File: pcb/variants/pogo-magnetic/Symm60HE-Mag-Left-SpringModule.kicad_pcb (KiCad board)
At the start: 2 copper layers, 32 x 18 mm, 2 parts

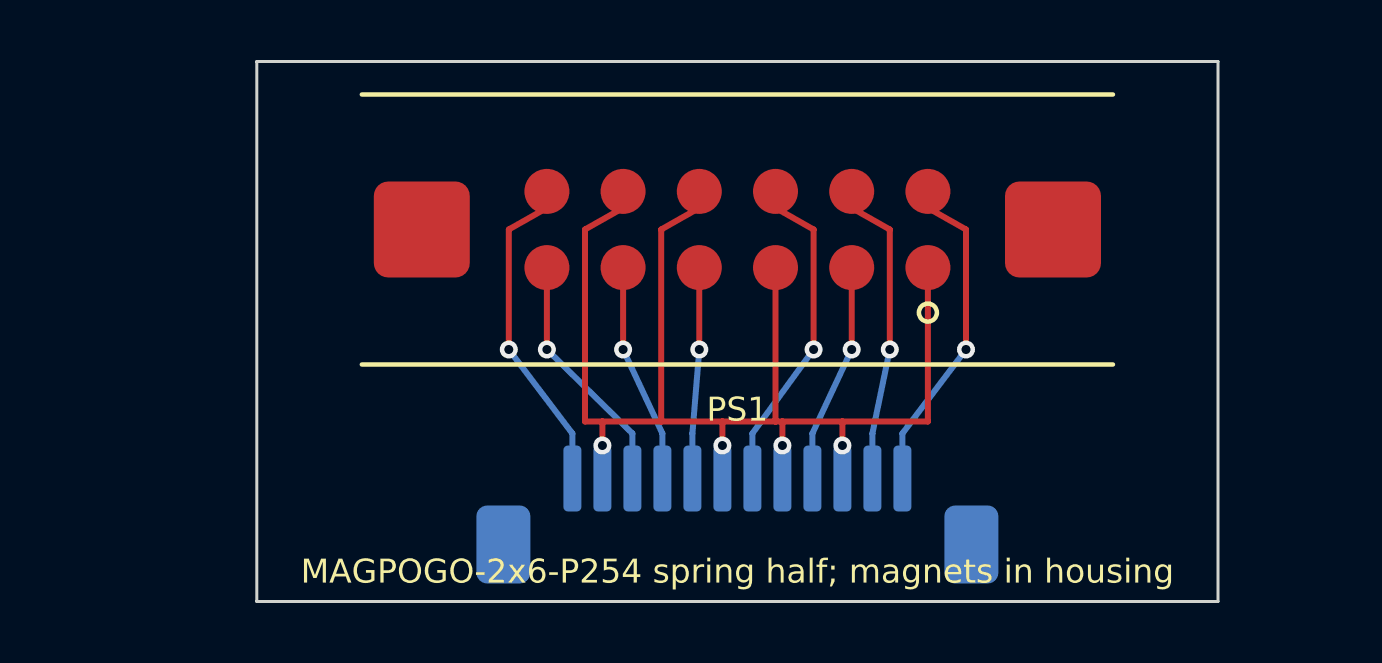
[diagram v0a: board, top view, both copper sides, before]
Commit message: Rebuild the magnetic variant around SUNMON 903-00081
Replaces the invented MAGPOGO-2x6-P254 interface drawing with a real part:
SUNMON 903-00081 / 904-00080 (MC142-09R), nine contacts in two staggered rows
on 1.50 mm pitch with 1.25 mm between rows, 1.20 mm contacts, 0.50 mm DIP
tails, and N52 magnets internal to the housing keyed N to S. Every footprint
dimension is read off the two published drawings.

Nine contacts is the link's functional minimum -- four ADC channels, three mux
selects, +3V3A and one ground -- so the twelve-way interface's four separate
grounds collapse to one and the module ties the controller ZIF's four ground
pads to that single contact.

The stagger is the hard part and it is the part's, not this attempt's:
diagonal neighbours are 1.458 mm apart with 1.25 mm pads, so nothing routes
between the contacts and every run leaves the array at its perimeter. The row
facing the ZIF drops straight to B.Cu; the other takes F.Cu over the top, down
the module side and back in above the ZIF.

Routing is not finished: 6 and 4 clearance flags on the modules, 11 on each
half. Recorded in the README along with why. Footprints, land pattern, pinout
and module outline are settled; the fanout is not.

Modules are 26 x 16 mm. docs/img/42 redraws them and docs/img/43 adds the
target breakout on the Hall PCBs.

Co-Authored-By: Claude Opus 5 <noreply@anthropic.com>
Claude-Session: https://claude.ai/code/session_01CRkZ4zVz5Mq7Fa3C5HAmii
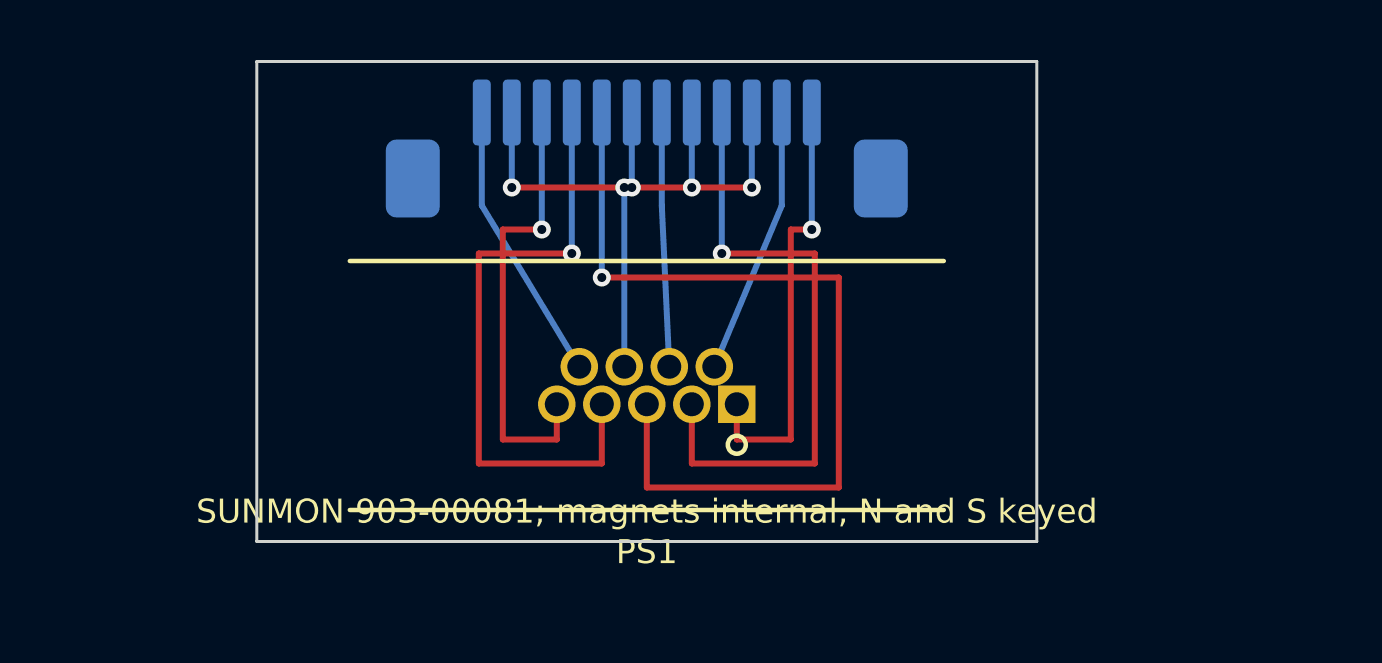
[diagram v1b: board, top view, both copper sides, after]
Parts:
- PS1: value MAGPOGO-2x6-P254-S -> 903-00081; footprint MagPogo_2x6_P254_Spring -> MagPogo_9_MC142_Spring
- moved JF1 12.6 mm to (13.0, 2.80)
- moved PS1 6.01 mm to (13.0, 10.8)
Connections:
- PS1 pad 1: GND -> ADC_L4
- PS1 pad 3: GND -> MUX_A2
- PS1 pad 4: MUX_A2 -> MUX_A1
- PS1 pad 5: MUX_A1 -> MUX_A0
- PS1 pad 6: MUX_A0 -> ADC_L3
- PS1 pad 7: ADC_L4 -> ADC_L1
- PS1 pad 8: ADC_L3 -> GND
- PS1 pad 9: ADC_L1 -> +3V3A
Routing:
- net MUX_A2: track 7.04 -> 29.6 mm
- net GND: track 46.1 -> 24.0 mm, vias 4 -> 5
- net ADC_L2: track 7.32 -> 20.9 mm
- net MUX_A1: track 7.32 -> 20.9 mm
- net MUX_A0: track 8.23 -> 15.2 mm
- net ADC_L4: track 11.0 -> 14.6 mm
- net ADC_L1: track 11.0 -> 8.48 mm, vias 1 -> 0
- net +3V3A: track 11.0 -> 9.38 mm, vias 1 -> 0
- net ADC_L3: track 10.4 -> 8.93 mm, vias 1 -> 0
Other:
- board size 32 x 18 mm -> 26 x 16 mm
- board text added: "SUNMON 903-00081; magnets internal, N and S keyed"
- board text removed: "MAGPOGO-2x6-P254 spring half; magnets in housing"
